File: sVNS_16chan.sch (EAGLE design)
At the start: 56 parts, among them IC2 OPA990IDCKR, IC3 EFM8SB10F2G-A-QFN20, J1 M50-3631042, J2 M50-3631042, J3 M50-3631042, U1 NT3H2211W0FHKH, U2 LT8410EDC-1#TRMPBF, U3 MUX36S16IRSNR, U4 MUX36S16IRSNR

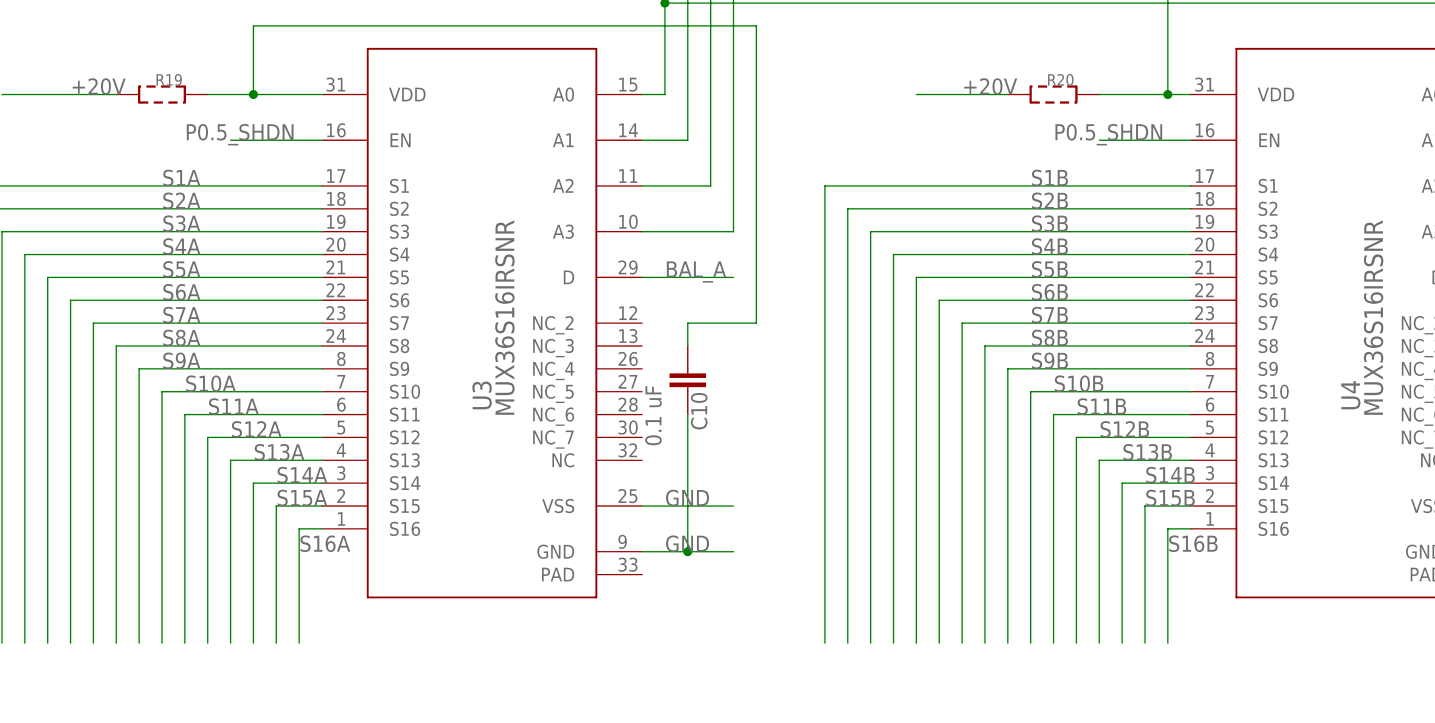
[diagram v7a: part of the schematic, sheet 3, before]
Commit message: Mapped output stage in the schematics
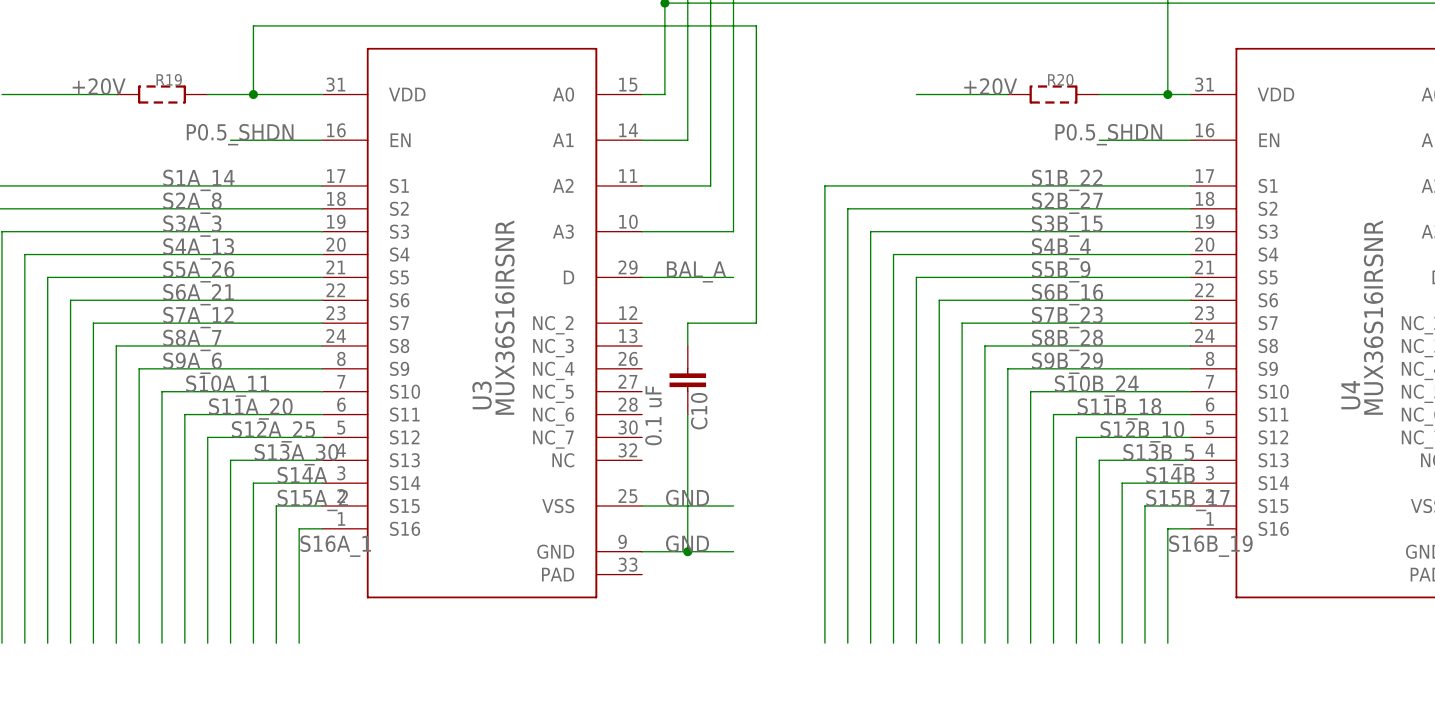
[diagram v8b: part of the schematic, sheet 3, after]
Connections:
- net S10A renamed S10A_11
- net S10B renamed S10B_24
- net S11A renamed S11A_20
- net S11B renamed S11B_18
- net S12A renamed S12A_25
- net S12B renamed S12B_10
- net S13A renamed S13A_30
- net S13B renamed S13B_5
- net S15A renamed S15A_2
- net S15B renamed S15B_17
- net S16A renamed S16A_1
- net S16B renamed S16B_19
- net S1A renamed S1A_14
- net S1B renamed S1B_22
- net S2A renamed S2A_8
- net S2B renamed S2B_27
- net S3A renamed S3A_3
- net S3B renamed S3B_15
- net S4A renamed S4A_13
- net S4B renamed S4B_4
- net S5A renamed S5A_26
- net S5B renamed S5B_9
- net S6A renamed S6A_21
- net S6B renamed S6B_16
- net S7A renamed S7A_12
- net S7B renamed S7B_23
- net S8A renamed S8A_7
- net S8B renamed S8B_28
- net S9A renamed S9A_6
- net S9B renamed S9B_29
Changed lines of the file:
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@@
 </busses>
 <nets>
-<net name="S16A" class="0">
+<net name="S16A_1" class="0">
 <segment>
 <pinref part="U3" gate="A" pin="S16"/>
@@
 </segment>
 </net>
-<net name="S15A" class="0">
+<net name="S15A_2" class="0">
 <segment>
 <pinref part="U3" gate="A" pin="S15"/>
@@
 </segment>
 </net>
-<net name="S13A" class="0">
+<net name="S13A_30" class="0">
 <segment>
 <pinref part="U3" gate="A" pin="S13"/>
@@
 </segment>
 </net>
-<net name="S12A" class="0">
+<net name="S12A_25" class="0">
 <segment>
 <pinref part="U3" gate="A" pin="S12"/>
@@
 </segment>
 </net>
-<net name="S11A" class="0">
+<net name="S11A_20" class="0">
 <segment>
 <pinref part="U3" gate="A" pin="S11"/>
@@
 </segment>
 </net>
-<net name="S10A" class="0">
+<net name="S10A_11" class="0">
 <segment>
 <pinref part="U3" gate="A" pin="S10"/>
@@
 </segment>
 </net>
-<net name="S9A" class="0">
+<net name="S9A_6" class="0">
 <segment>
 <pinref part="U3" gate="A" pin="S9"/>
@@
 </segment>
 </net>
-<net name="S8A" class="0">
+<net name="S8A_7" class="0">
 <segment>
 <pinref part="U3" gate="A" pin="S8"/>
@@
 </segment>
 </net>
-<net name="S7A" class="0">
+<net name="S7A_12" class="0">
 <segment>
 <pinref part="U3" gate="A" pin="S7"/>
@@
 </segment>
 </net>
-<net name="S6A" class="0">
+<net name="S6A_21" class="0">
 <segment>
 <pinref part="U3" gate="A" pin="S6"/>
@@
 </segment>
 </net>
-<net name="S5A" class="0">
+<net name="S5A_26" class="0">
 <segment>
 <pinref part="U3" gate="A" pin="S5"/>
@@
 </segment>
 </net>
-<net name="S4A" class="0">
+<net name="S4A_13" class="0">
 <segment>
 <pinref part="U3" gate="A" pin="S4"/>
@@
 </segment>
 </net>
-<net name="S3A" class="0">
+<net name="S3A_3" class="0">
 <segment>
 <pinref part="U3" gate="A" pin="S3"/>
@@
 </segment>
 </net>
-<net name="S2A" class="0">
+<net name="S2A_8" class="0">
 <segment>
 <pinref part="U3" gate="A" pin="S2"/>
@@
 </segment>
 </net>
-<net name="S1A" class="0">
+<net name="S1A_14" class="0">
 <segment>
 <pinref part="U3" gate="A" pin="S1"/>
@@
 </segment>
 </net>
-<net name="S16B" class="0">
+<net name="S16B_19" class="0">
 <segment>
 <wire x1="175.26" y1="91.44" x2="172.72" y2="91.44" width="0.1524" layer="91"/>
@@
 </segment>
 </net>
-<net name="S15B" class="0">
+<net name="S15B_17" class="0">
 <segment>
 <wire x1="175.26" y1="93.98" x2="170.18" y2="93.98" width="0.1524" layer="91"/>
@@
 </segment>
 </net>
-<net name="S13B" class="0">
+<net name="S13B_5" class="0">
 <segment>
 <wire x1="175.26" y1="99.06" x2="165.1" y2="99.06" width="0.1524" layer="91"/>
@@
 </segment>
 </net>
-<net name="S12B" class="0">
+<net name="S12B_10" class="0">
 <segment>
 <wire x1="175.26" y1="101.6" x2="162.56" y2="101.6" width="0.1524" layer="91"/>
@@
 </segment>
 </net>
-<net name="S11B" class="0">
+<net name="S11B_18" class="0">
 <segment>
 <wire x1="175.26" y1="104.14" x2="160.02" y2="104.14" width="0.1524" layer="91"/>
@@
 </segment>
 </net>
-<net name="S10B" class="0">
+<net name="S10B_24" class="0">
 <segment>
 <wire x1="175.26" y1="106.68" x2="157.48" y2="106.68" width="0.1524" layer="91"/>
@@
 </segment>
 </net>
-<net name="S9B" class="0">
+<net name="S9B_29" class="0">
 <segment>
 <wire x1="175.26" y1="109.22" x2="154.94" y2="109.22" width="0.1524" layer="91"/>
@@
 </segment>
 </net>
-<net name="S8B" class="0">
+<net name="S8B_28" class="0">
 <segment>
 <wire x1="175.26" y1="111.76" x2="152.4" y2="111.76" width="0.1524" layer="91"/>
@@
 </segment>
 </net>
-<net name="S7B" class="0">
+<net name="S7B_23" class="0">
 <segment>
 <wire x1="175.26" y1="114.3" x2="149.86" y2="114.3" width="0.1524" layer="91"/>
@@
 </segment>
 </net>
-<net name="S6B" class="0">
+<net name="S6B_16" class="0">
 <segment>
 <wire x1="175.26" y1="116.84" x2="147.32" y2="116.84" width="0.1524" layer="91"/>
@@
 </segment>
 </net>
-<net name="S5B" class="0">
+<net name="S5B_9" class="0">
 <segment>
 <wire x1="175.26" y1="119.38" x2="144.78" y2="119.38" width="0.1524" layer="91"/>
@@
 </segment>
 </net>
-<net name="S4B" class="0">
+<net name="S4B_4" class="0">
 <segment>
 <wire x1="175.26" y1="121.92" x2="142.24" y2="121.92" width="0.1524" layer="91"/>
@@
 </segment>
 </net>
-<net name="S3B" class="0">
+<net name="S3B_15" class="0">
 <segment>
 <wire x1="175.26" y1="124.46" x2="139.7" y2="124.46" width="0.1524" layer="91"/>
@@
 </segment>
 </net>
-<net name="S2B" class="0">
+<net name="S2B_27" class="0">
 <segment>
 <wire x1="175.26" y1="127" x2="137.16" y2="127" width="0.1524" layer="91"/>
@@
 </segment>
 </net>
-<net name="S1B" class="0">
+<net name="S1B_22" class="0">
 <segment>
 <wire x1="175.26" y1="129.54" x2="134.62" y2="129.54" width="0.1524" layer="91"/>
